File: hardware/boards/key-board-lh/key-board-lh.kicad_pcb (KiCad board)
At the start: 2 copper layers, 79 x 39 mm, 24 parts

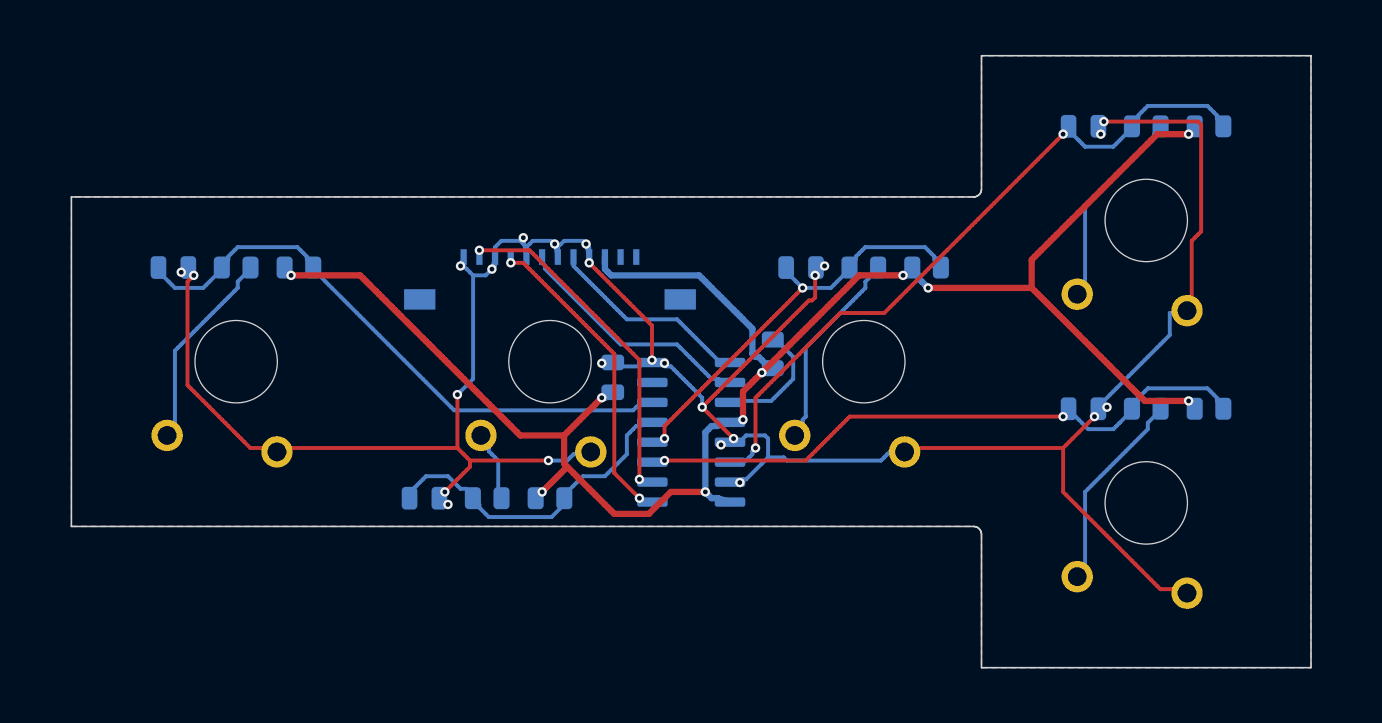
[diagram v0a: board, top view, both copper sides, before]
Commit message: Key boards screw to the key plate; LH board gets standoff holes and keep-outs
The owner's choice (ADR 0020): each key board is held to the plate's
underside by M2 self-clinching standoffs pressed into the plate and M2
screws up through the board, instead of hanging on its switches' solder
joints. The ribbon connector envelope takes the Molex 200528 footprint's
size; the board stays the same size.

- CAD: kb_standoffs() places one between neighbouring switches wherever the
  plate's web holds it (2 on the left hand, 3 on the right); the standoff
  length is derived from switch.pcb_below_seat and printed in drc.echo; the
  plate DXF gets the holes; the placeholder parts envelope keeps clear of
  the screw heads. 0 DRC FAILs, 0 clashes.
- PCB: tools/pcb.py places NPTH holes from pcb-geometry.echo, with a copper
  keep-out on both layers under the standoff face and the screw head, so
  the plate makes no second ground bond; check fails if a hole leaves the
  CAD's position. The router treats keep-outs as obstacles, checks a
  stitching via's stub for clearance before laying it, and still joins the
  ground pins its main tree cannot reach. LH board: DRC 0 errors, parity
  clean, renders and fab/ regenerated.
- BOM: MECH-KB-STANDOFF and MECH-KB-SCREW in hardware/unplaced.csv.
- Docs: ADR 0020 and index; cluster-boards.md, mechanical/DESIGN.md and
  tooling.md say how the boards are held.

Co-Authored-By: Claude Opus 5.5 <noreply@anthropic.com>
Claude-Session: https://claude.ai/code/session_01LmB4muFXnoLprWX4JzuJ5A
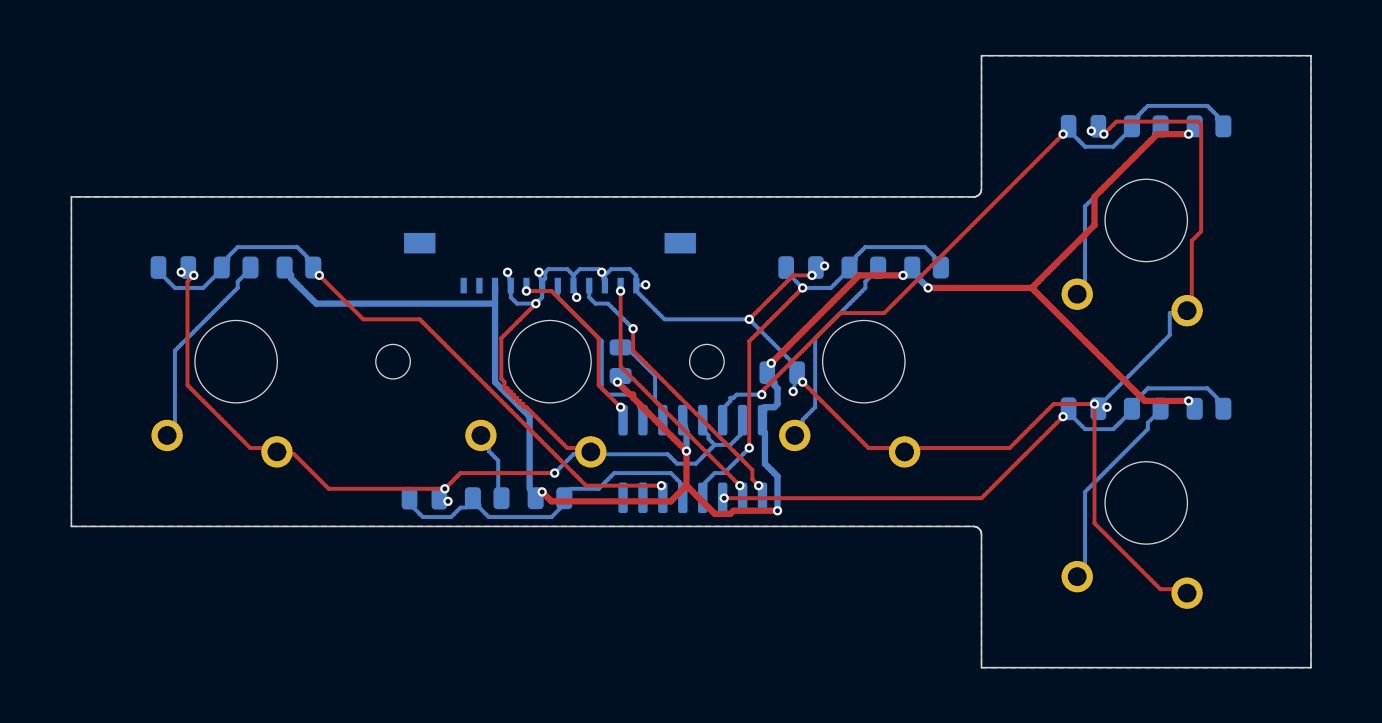
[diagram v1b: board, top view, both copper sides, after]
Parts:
- added H1: M2 standoff, MountingHole:MountingHole_2.2mm_M2, B.Cu at (120.0, 121.5)
- added H2: M2 standoff, MountingHole:MountingHole_2.2mm_M2, B.Cu at (140.0, 121.5)
- moved C-DECOUPLE-165-LH 10.8 mm to (144.8, 122.2), turned to 0 degrees
- moved R-KEY-PU-FREE3 9.71 mm to (134.5, 121.5)
- moved U-KEYS-LH 1.70 mm to (139.1, 127.7), turned to 90 degrees
- turned J-CHAIN to 0 degrees
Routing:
- net /CHAIN_SCK: track 21.5 -> 15.9 mm
- net /CHAIN_SER_LH: track 15.2 -> 11.2 mm
- net GND_CHAIN: track 168.0 -> 164.4 mm, vias 25 -> 20
- net /KEY_LH4: track 38.6 -> 35.1 mm
- net V3V3_CHAIN_LH: track 117.0 -> 113.7 mm, vias 10 -> 9
- net /KEY_LH1: track 36.1 -> 39.3 mm, vias 0 -> 2
- net /KEY_LH3: track 25.3 -> 27.5 mm
- net /KEY_FREE3: track 7.14 -> 5.06 mm
- net /KEY_LH5: track 43.1 -> 41.1 mm
- net /CHAIN_SHLD: track 19.2 -> 17.7 mm
- net /HOP_LH_LT: track 12.3 -> 11.2 mm, vias 0 -> 2
- net /KEY_LH2: track 18.8 -> 19.7 mm

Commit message: Key boards: 1.2 mm rectangles with a standoff in each corner; tidier routing
The owner's amendment to ADR 0020: standoffs "from the outside... anchor it
maybe in each corner", with the board grown to fit them and to give the
register room; and 1.2 mm boards, so the KS-33's pins show ~0.5 mm to solder
instead of ~0.1.

- CAD: a key board is a rectangle across the cavity (side walls less
  board_clear) and past its outermost cutouts by boards.kb_end_margin, with a
  standoff hardware.kb_standoff_inset in from each corner. New rule "key
  boards clear of the lid screws"; the ribbon's run under the board is kept
  out of the parts envelope and exported as a no-parts strip. Key boards take
  boards.key_board_t (the main board keeps switch.pcb_t, to be decided with
  its layout). 0 DRC FAILs, 0 clashes.
- PCB: the ribbon strip is a no-footprints rule area. The router gets a
  preferred direction per layer, angle-graded turn costs and a rip-up and
  reroute pass. LH board re-placed: the register on the far side with its
  inputs facing the keys in order. DRC 0 errors, parity clean; renders and
  fab/ regenerated.
- BOM: PCB-CLUSTER 1.2 mm; MECH-KB-STANDOFF and MECH-KB-SCREW 8 each.
- Docs: ADR 0020 amended (points 3 and 6); cluster-boards.md, DESIGN.md,
  tooling.md follow.

Co-Authored-By: Claude Opus 5.5 <noreply@anthropic.com>
Claude-Session: https://claude.ai/code/session_01LmB4muFXnoLprWX4JzuJ5A
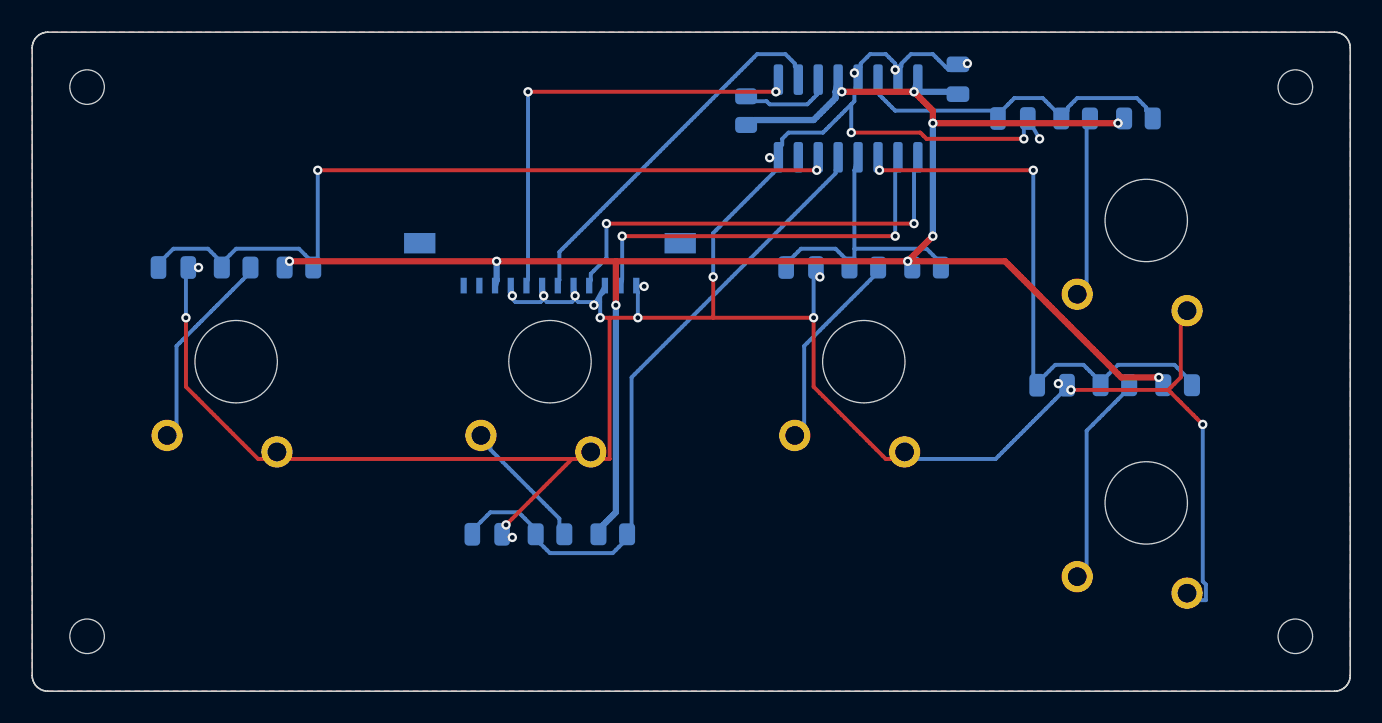
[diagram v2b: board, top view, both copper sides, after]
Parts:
- added H3: M2 standoff, MountingHole:MountingHole_2.2mm_M2, B.Cu at (177.5, 139.0)
- added H4: M2 standoff, MountingHole:MountingHole_2.2mm_M2, B.Cu at (177.5, 104.0)
- moved H2 43.2 mm to (100.5, 104.0)
- moved H1 26.2 mm to (100.5, 139.0)
- moved U-KEYS-LH 23.9 mm to (149.0, 106.0)
- moved C-DECOUPLE-165-LH 21.8 mm to (156.0, 103.5), turned to 90 degrees
- moved R-KEY-PU-FREE3 17.9 mm to (142.5, 105.5)
- moved C-KEY-LH2 4.61 mm to (126.0, 132.5)
- moved R-KEY-PU-LH2 4.61 mm to (134.0, 132.5)
- moved R-KEY-SER-LH2 4.61 mm to (130.0, 132.5)
- moved C-KEY-LH5 4.53 mm to (159.5, 106.0)
- moved R-KEY-PU-LH5 4.53 mm to (167.5, 106.0)
- moved R-KEY-SER-LH5 4.53 mm to (163.5, 106.0)
- moved C-KEY-LH4 2.50 mm to (162.0, 123.0)
- moved R-KEY-PU-LH4 2.50 mm to (170.0, 123.0)
- moved R-KEY-SER-LH4 2.50 mm to (166.0, 123.0)
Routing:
- net /KEY_LH5: track 41.1 -> 19.8 mm, vias 2 -> 0
- net /KEY_LH2: track 19.7 -> 40.0 mm
- net GND_CHAIN: track 164.4 -> 183.3 mm, vias 20 -> 24
- net /HOP_LH_LT: track 11.2 -> 28.6 mm
- net /CHAIN_SER_LH: track 11.2 -> 22.8 mm
- net /KEY_LH3: track 27.5 -> 17.2 mm, vias 2 -> 0
- net /KEY_LH1: track 39.3 -> 49.2 mm
- net /CHAIN_SHLD: track 17.7 -> 27.4 mm
- net /CHAIN_SCK: track 15.9 -> 24.8 mm
- net V3V3_CHAIN_LH: track 113.7 -> 118.5 mm, vias 9 -> 10
- net /LH2/SWITCH_LEG: track 3.79 -> 7.74 mm
- net /LH5/SWITCH_LEG: track 11.9 -> 10.5 mm
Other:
- board size 79 x 39 mm -> 84 x 42 mm

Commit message: Key chain on through-hole 1.27 mm IDC: model, key boards, router fix
The owner's choice (option 2): a right-angle 2x6 1.27 mm shrouded IDC header
on each board (Samtec SHF-106-01-L-D-RA stand-in), the key board's hanging
over the main board's, and a flat IDC ribbon long enough to plug in with the
lid laid beside the body - closed, a flat hairpin along the body, clear of
the LED strip.

- CAD: chain headers, plugs and the hairpin ribbon replace the ZIF/FFC C;
  positions found clear of every switch's pole and pins and the regulator
  block; ribbon length derived from the service position (drc.echo); a plate
  window over the key header's pin tails. body.yaml boards.chain_* and
  routing.chain_* replace ffc_*. 0 DRC FAILs, 0 clashes over 134 solids.
- Key boards: J-CHAIN footprint woody:IDC-Header_2x06_P1.27mm_Samtec_SHF_
  Horizontal (new); pinout moved one pin for the upside-down header (main
  pin n -> key pin 12-n odd / 14-n even); ERC clean. The interface netlist
  follows and agrees pin for pin.
- pcb.py places J-CHAIN from the CAD's "chain" line and checks it; the
  router no longer walls a plated pad off from its own track (1.27 mm pads).
  LH board: DRC 0 errors, parity clean; renders and fab/ regenerated.

The BOM rows, the key-chain page and the ADR 0017 amendment follow in the
next commit.

Co-Authored-By: Claude Opus 5.5 <noreply@anthropic.com>
Claude-Session: https://claude.ai/code/session_01LmB4muFXnoLprWX4JzuJ5A
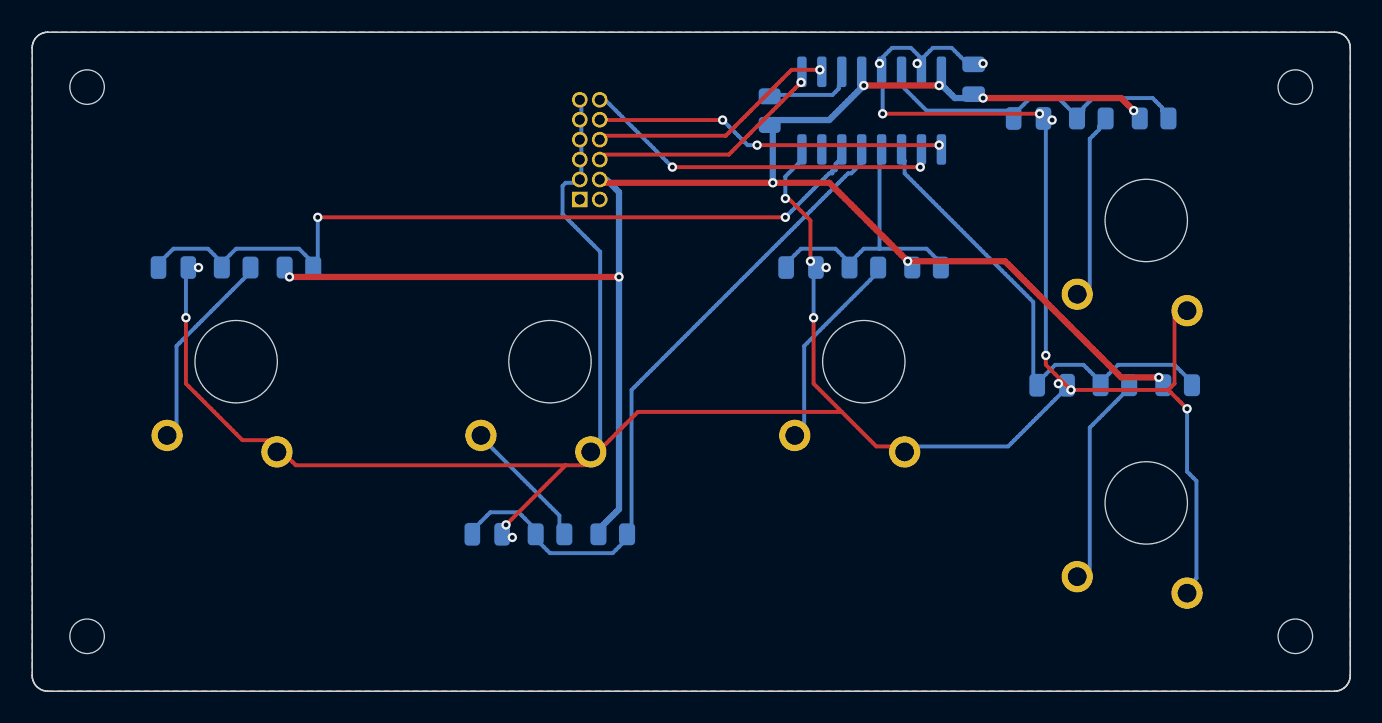
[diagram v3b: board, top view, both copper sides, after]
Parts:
- removed the J-CHAIN at (130.0, 115.7)
- added J-CHAIN: 12-way, woody:IDC-Header_2x06_P1.27mm_Samtec_SHF_Horizontal, B.Cu at (131.9, 111.2)
- moved U-KEYS-LH 1.58 mm to (150.5, 105.5)
- moved R-KEY-PU-FREE3 1.50 mm to (144.0, 105.5)
- moved C-DECOUPLE-165-LH 1.00 mm to (157.0, 103.5)
- moved C-KEY-LH5 1.00 mm to (160.5, 106.0)
- moved R-KEY-PU-LH5 1.00 mm to (168.5, 106.0)
- moved R-KEY-SER-LH5 1.00 mm to (164.5, 106.0)
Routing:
- net /HOP_LH_LT: track 28.6 -> 15.2 mm, vias 2 -> 1
- net /CHAIN_SER_LH: track 22.8 -> 15.7 mm, vias 0 -> 1
- net /KEY_LH4: track 34.9 -> 29.0 mm, vias 2 -> 0
- net /CHAIN_SHLD: track 27.4 -> 22.3 mm, vias 2 -> 3
- net V3V3_CHAIN_LH: track 118.5 -> 116.2 mm, vias 10 -> 9
- net /CHAIN_SCK: track 24.8 -> 22.9 mm
- net /KEY_LH2: track 40.0 -> 41.2 mm
- net /LH5/SWITCH_LEG: track 10.5 -> 11.1 mm
- net /KEY_FREE3: track 5.31 -> 4.77 mm
- net GND_CHAIN: track 183.3 -> 182.8 mm, vias 24 -> 18

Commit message: LH key board as the worked example: orderable, labelled, testable
- Samtec full prints banked (SHF header, FFSD cable); the header's true
  dimensions replace the catalogue estimates (body.yaml boards.chain_*), and
  the cable is ordered -RN2 (notch reversed on the key-board end): both
  sockets' cables leave downward, the ribbon runs flat, and key-board pin =
  13 - main-board pin. The same-day 12-n/14-n map was wrong and is undone in
  the sheets, the interface netlist and the docs (history in notes.md).
- Model: the hairpin's legs follow the cable's real exit - the main board's
  on the board, clear of the thumb switches' poles; 0 DRC FAILs, 0 clashes.
- Sheets: Manufacturer/MPN/LCSC/Assembly fields from JLC's parts API (JLC
  and LCSC pages banked in datasheets/fab and the manifest); five bring-up
  test pads per key board (TP-CHAIN, copper only).
- pcb.py: JLC's limits in the DRC (layout.yaml fab:), which grew the vias
  and J-CHAIN's pads to the 0.18 mm ring; HASL lead-free in the stackup and
  Gerber job; a generated parts-side silkscreen; the JLC BOM, CPL and
  hand-assembly list in fab/, ledgered against board and sheets.
- Router: a real rip-up (blockers removed too); plated holes no longer wall
  off their own pads.
- hardware/boards/key-board-lh/README.md: sources, ordering, hand assembly,
  bring-up, open items. tooling.md and lib README follow.
All checks pass: CAD, DRC (0/0), KiCad, staleness, BOM, netlist, datasheets.

Co-Authored-By: Claude Opus 5.5 <noreply@anthropic.com>
Claude-Session: https://claude.ai/code/session_01LmB4muFXnoLprWX4JzuJ5A
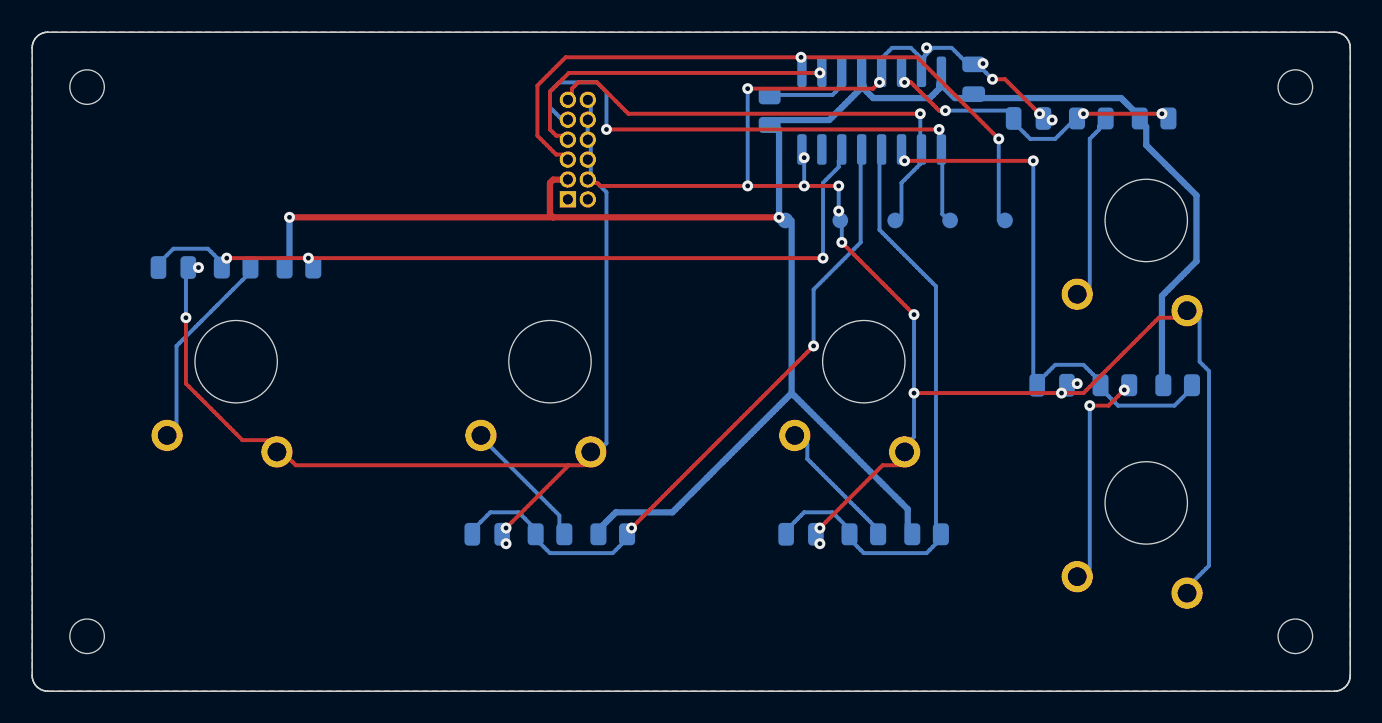
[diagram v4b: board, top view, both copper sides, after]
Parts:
- added TP-3V3-LH: test pad, TestPoint:TestPoint_Pad_D1.0mm, B.Cu at (145.0, 112.5)
- added TP-GND-LH: test pad, TestPoint:TestPoint_Pad_D1.0mm, B.Cu at (148.5, 112.5)
- added TP-QH-LH: test pad, TestPoint:TestPoint_Pad_D1.0mm, B.Cu at (159.0, 112.5)
- added TP-SCK-LH: test pad, TestPoint:TestPoint_Pad_D1.0mm, B.Cu at (152.0, 112.5)
- added TP-SHLD-LH: test pad, TestPoint:TestPoint_Pad_D1.0mm, B.Cu at (155.5, 112.5)
- moved C-KEY-LH3 17.0 mm to (146.0, 132.5)
- moved R-KEY-PU-LH3 17.0 mm to (154.0, 132.5)
- moved R-KEY-SER-LH3 17.0 mm to (150.0, 132.5)
- moved J-CHAIN 0.76 mm to (131.1, 111.2)
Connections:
- J-CHAIN pad 10: /CHAIN_SHLD -> GND_CHAIN
- J-CHAIN pad 11: GND_CHAIN -> /CHAIN_SCK
- J-CHAIN pad 12: /CHAIN_SCK -> GND_CHAIN
- J-CHAIN pad 3: GND_CHAIN -> V3V3_CHAIN_LH
- J-CHAIN pad 4: V3V3_CHAIN_LH -> GND_CHAIN
- J-CHAIN pad 5: GND_CHAIN -> /HOP_LH_LT
- J-CHAIN pad 6: /HOP_LH_LT -> GND_CHAIN
- J-CHAIN pad 7: GND_CHAIN -> /CHAIN_SER_LH
- J-CHAIN pad 8: /CHAIN_SER_LH -> GND_CHAIN
- J-CHAIN pad 9: GND_CHAIN -> /CHAIN_SHLD
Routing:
- net /HOP_LH_LT: track 15.2 -> 43.9 mm, vias 1 -> 2
- net /KEY_LH3: track 17.3 -> 36.6 mm
- net V3V3_CHAIN_LH: track 116.2 -> 129.1 mm, vias 9 -> 2
- net /CHAIN_SHLD: track 22.3 -> 34.6 mm, vias 3 -> 2
- net /CHAIN_SCK: track 22.9 -> 30.4 mm, vias 2 -> 1
- net /CHAIN_SER_LH: track 15.7 -> 21.5 mm
- net /KEY_LH4: track 29.0 -> 33.8 mm, vias 0 -> 2
- net /LH3/SWITCH_LEG: track 12.1 -> 7.62 mm
- net GND_CHAIN: track 182.8 -> 179.6 mm, vias 18 -> 23
- net /KEY_LH5: track 19.5 -> 18.2 mm, vias 0 -> 4
- net /KEY_LH1: track 49.4 -> 50.6 mm, vias 2 -> 3
- net /LH4/SWITCH_LEG: track 12.7 -> 13.4 mm, vias 0 -> 2
- net /KEY_LH2: track 41.2 -> 41.3 mm, vias 0 -> 2
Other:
- board text added: "3V3"
- board text added: "74HC165"
- board text added: "C"
- board text added: "CD"
- board text added: "GND"
- board text added: "J-CHAIN"
- board text added: "LH1"
- board text added: "LH2"
- board text added: "LH3"
- board text added: "LH4"
- board text added: "LH5"
- board text added: "P"
- board text added: "PF"
- board text added: "QH"
- board text added: "S"
- board text added: "SCK"
- board text added: "SH/LD"
- board text added: "WOODY key board LH"
- board text added: "rev A 2026-09-27"
